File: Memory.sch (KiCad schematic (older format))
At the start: 20 parts, among them U10 DRAM_4464, U9 DRAM_4464

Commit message: SMD ram
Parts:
- R100, R101, R102, R103, R104, R105, R106, R107, R207, R208, R209, R210, R211, R212, R213, R214: footprint Atari:R_Axial_DIN0207_L3.6mm_D2.2mm_P10.16mm_Horizontal -> Resistor_SMD:R_1206_3216Metric_Pad1.42x1.75mm_HandSolder
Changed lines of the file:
@@
 F 0 "R207" V 2800 1175 50  0000 C CNN
 F 1 "33" V 2800 1350 50  0000 C CNN
-F 2 "Atari:R_Axial_DIN0207_L3.6mm_D2.2mm_P10.16mm_Horizontal" V 2830 1325 50  0001 C CNN
+F 2 "Resistor_SMD:R_1206_3216Metric_Pad1.42x1.75mm_HandSolder" V 2830 1325 50  0001 C CNN
 F 3 "~" H 2900 1325 50  0001 C CNN
 	1    2900 1325
@@
 F 0 "R208" V 2800 1350 50  0000 C CNN
 F 1 "33" V 2800 1525 50  0000 C CNN
-F 2 "Atari:R_Axial_DIN0207_L3.6mm_D2.2mm_P10.16mm_Horizontal" V 2830 1500 50  0001 C CNN
+F 2 "Resistor_SMD:R_1206_3216Metric_Pad1.42x1.75mm_HandSolder" V 2830 1500 50  0001 C CNN
 F 3 "~" H 2900 1500 50  0001 C CNN
 	1    2900 1500
@@
 F 0 "R209" V 2800 1550 50  0000 C CNN
 F 1 "33" V 2800 1725 50  0000 C CNN
-F 2 "Atari:R_Axial_DIN0207_L3.6mm_D2.2mm_P10.16mm_Horizontal" V 2830 1700 50  0001 C CNN
+F 2 "Resistor_SMD:R_1206_3216Metric_Pad1.42x1.75mm_HandSolder" V 2830 1700 50  0001 C CNN
 F 3 "~" H 2900 1700 50  0001 C CNN
 	1    2900 1700
@@
 F 0 "R210" V 2800 1750 50  0000 C CNN
 F 1 "33" V 2800 1925 50  0000 C CNN
-F 2 "Atari:R_Axial_DIN0207_L3.6mm_D2.2mm_P10.16mm_Horizontal" V 2830 1900 50  0001 C CNN
+F 2 "Resistor_SMD:R_1206_3216Metric_Pad1.42x1.75mm_HandSolder" V 2830 1900 50  0001 C CNN
 F 3 "~" H 2900 1900 50  0001 C CNN
 	1    2900 1900
@@
 F 0 "R211" V 2800 1950 50  0000 C CNN
 F 1 "33" V 2800 2125 50  0000 C CNN
-F 2 "Atari:R_Axial_DIN0207_L3.6mm_D2.2mm_P10.16mm_Horizontal" V 2830 2100 50  0001 C CNN
+F 2 "Resistor_SMD:R_1206_3216Metric_Pad1.42x1.75mm_HandSolder" V 2830 2100 50  0001 C CNN
 F 3 "~" H 2900 2100 50  0001 C CNN
 	1    2900 2100
@@
 F 0 "R212" V 2800 2150 50  0000 C CNN
 F 1 "33" V 2800 2325 50  0000 C CNN
-F 2 "Atari:R_Axial_DIN0207_L3.6mm_D2.2mm_P10.16mm_Horizontal" V 2830 2300 50  0001 C CNN
+F 2 "Resistor_SMD:R_1206_3216Metric_Pad1.42x1.75mm_HandSolder" V 2830 2300 50  0001 C CNN
 F 3 "~" H 2900 2300 50  0001 C CNN
 	1    2900 2300
@@
 F 0 "R213" V 2800 2350 50  0000 C CNN
 F 1 "33" V 2800 2525 50  0000 C CNN
-F 2 "Atari:R_Axial_DIN0207_L3.6mm_D2.2mm_P10.16mm_Horizontal" V 2830 2500 50  0001 C CNN
+F 2 "Resistor_SMD:R_1206_3216Metric_Pad1.42x1.75mm_HandSolder" V 2830 2500 50  0001 C CNN
 F 3 "~" H 2900 2500 50  0001 C CNN
 	1    2900 2500
@@
 F 0 "R214" V 2800 2550 50  0000 C CNN
 F 1 "33" V 2800 2725 50  0000 C CNN
-F 2 "Atari:R_Axial_DIN0207_L3.6mm_D2.2mm_P10.16mm_Horizontal" V 2830 2700 50  0001 C CNN
+F 2 "Resistor_SMD:R_1206_3216Metric_Pad1.42x1.75mm_HandSolder" V 2830 2700 50  0001 C CNN
 F 3 "~" H 2900 2700 50  0001 C CNN
 	1    2900 2700
@@
 F 0 "R100" V 2925 3775 50  0000 C CNN
 F 1 "10k" V 2875 3600 50  0000 C CNN
-F 2 "Atari:R_Axial_DIN0207_L3.6mm_D2.2mm_P10.16mm_Horizontal" V 2855 3775 50  0001 C CNN
+F 2 "Resistor_SMD:R_1206_3216Metric_Pad1.42x1.75mm_HandSolder" V 2855 3775 50  0001 C CNN
 F 3 "~" H 2925 3775 50  0001 C CNN
 	1    2925 3775
@@
 F 0 "R101" V 2925 3900 50  0000 C CNN
 F 1 "10k" V 2875 3725 50  0000 C CNN
-F 2 "Atari:R_Axial_DIN0207_L3.6mm_D2.2mm_P10.16mm_Horizontal" V 2855 3900 50  0001 C CNN
+F 2 "Resistor_SMD:R_1206_3216Metric_Pad1.42x1.75mm_HandSolder" V 2855 3900 50  0001 C CNN
 F 3 "~" H 2925 3900 50  0001 C CNN
 	1    2925 3900
@@
 F 0 "R102" V 2925 4025 50  0000 C CNN
 F 1 "10k" V 2875 3850 50  0000 C CNN
-F 2 "Atari:R_Axial_DIN0207_L3.6mm_D2.2mm_P10.16mm_Horizontal" V 2855 4025 50  0001 C CNN
+F 2 "Resistor_SMD:R_1206_3216Metric_Pad1.42x1.75mm_HandSolder" V 2855 4025 50  0001 C CNN
 F 3 "~" H 2925 4025 50  0001 C CNN
 	1    2925 4025
@@
 F 0 "R103" V 2925 4150 50  0000 C CNN
 F 1 "10k" V 2875 3975 50  0000 C CNN
-F 2 "Atari:R_Axial_DIN0207_L3.6mm_D2.2mm_P10.16mm_Horizontal" V 2855 4150 50  0001 C CNN
+F 2 "Resistor_SMD:R_1206_3216Metric_Pad1.42x1.75mm_HandSolder" V 2855 4150 50  0001 C CNN
 F 3 "~" H 2925 4150 50  0001 C CNN
 	1    2925 4150
@@
 F 0 "R104" V 2925 4275 50  0000 C CNN
 F 1 "10k" V 2875 4100 50  0000 C CNN
-F 2 "Atari:R_Axial_DIN0207_L3.6mm_D2.2mm_P10.16mm_Horizontal" V 2855 4275 50  0001 C CNN
+F 2 "Resistor_SMD:R_1206_3216Metric_Pad1.42x1.75mm_HandSolder" V 2855 4275 50  0001 C CNN
 F 3 "~" H 2925 4275 50  0001 C CNN
 	1    2925 4275
@@
 F 0 "R105" V 2925 4400 50  0000 C CNN
 F 1 "10k" V 2875 4225 50  0000 C CNN
-F 2 "Atari:R_Axial_DIN0207_L3.6mm_D2.2mm_P10.16mm_Horizontal" V 2855 4400 50  0001 C CNN
+F 2 "Resistor_SMD:R_1206_3216Metric_Pad1.42x1.75mm_HandSolder" V 2855 4400 50  0001 C CNN
 F 3 "~" H 2925 4400 50  0001 C CNN
 	1    2925 4400
@@
 F 0 "R106" V 2925 4525 50  0000 C CNN
 F 1 "10k" V 2875 4350 50  0000 C CNN
-F 2 "Atari:R_Axial_DIN0207_L3.6mm_D2.2mm_P10.16mm_Horizontal" V 2855 4525 50  0001 C CNN
+F 2 "Resistor_SMD:R_1206_3216Metric_Pad1.42x1.75mm_HandSolder" V 2855 4525 50  0001 C CNN
 F 3 "~" H 2925 4525 50  0001 C CNN
 	1    2925 4525
@@
 F 0 "R107" V 2925 4650 50  0000 C CNN
 F 1 "10k" V 2875 4475 50  0000 C CNN
-F 2 "Atari:R_Axial_DIN0207_L3.6mm_D2.2mm_P10.16mm_Horizontal" V 2855 4650 50  0001 C CNN
+F 2 "Resistor_SMD:R_1206_3216Metric_Pad1.42x1.75mm_HandSolder" V 2855 4650 50  0001 C CNN
 F 3 "~" H 2925 4650 50  0001 C CNN
 	1    2925 4650

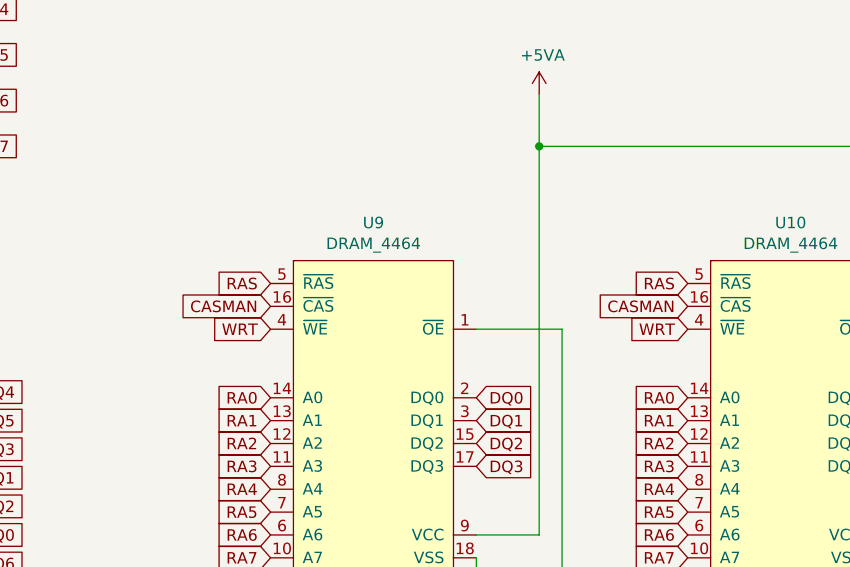
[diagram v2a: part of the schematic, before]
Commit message: add 74ls04
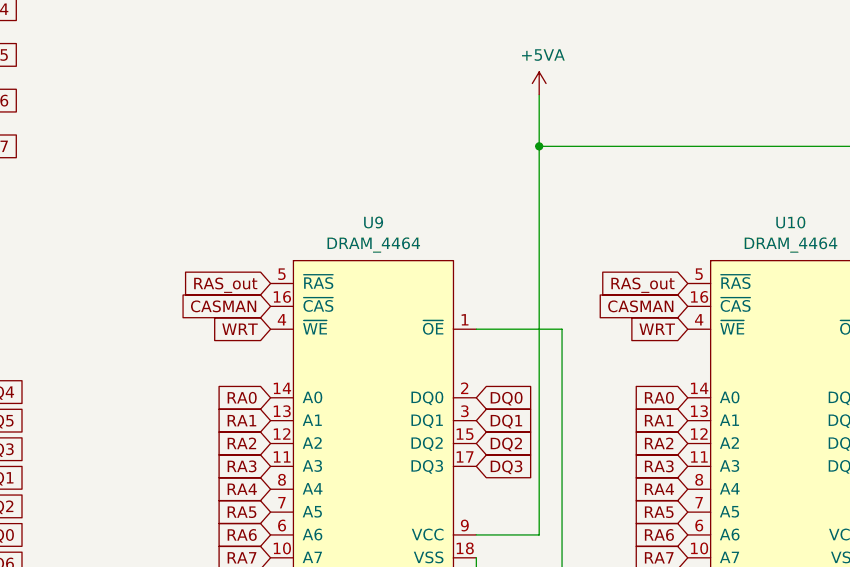
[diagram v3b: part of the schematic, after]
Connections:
- net RAS renamed RAS_out
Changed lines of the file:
@@
 $EndComp
 Text GLabel 4400 3300 0    50   Input ~ 0
-RAS
+RAS_out
 Text GLabel 4400 3500 0    50   Input ~ 0
 WRT
@@
 WRT
 Text GLabel 6225 3300 0    50   Input ~ 0
-RAS
+RAS_out
 Text GLabel 5300 3800 2    50   Input ~ 0
 DQ0

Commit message: Final inspection
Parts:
- C36, C37: footprint Capacitor_THT:C_Axial_L3.8mm_D2.6mm_P7.50mm_Horizontal -> Capacitor_SMD:C_1206_3216Metric_Pad1.42x1.75mm_HandSolder
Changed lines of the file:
@@
 F 0 "C37" H 6190 6096 50  0000 L CNN
 F 1 "100nF" H 6190 6005 50  0000 L CNN
-F 2 "Capacitor_THT:C_Axial_L3.8mm_D2.6mm_P7.50mm_Horizontal" H 6113 5900 50  0001 C CNN
+F 2 "Capacitor_SMD:C_1206_3216Metric_Pad1.42x1.75mm_HandSolder" H 6113 5900 50  0001 C CNN
 F 3 "~" H 6075 6050 50  0001 C CNN
 	1    6075 6050
@@
 F 0 "C36" H 6690 6096 50  0000 L CNN
 F 1 "100nF" H 6690 6005 50  0000 L CNN
-F 2 "Capacitor_THT:C_Axial_L3.8mm_D2.6mm_P7.50mm_Horizontal" H 6613 5900 50  0001 C CNN
+F 2 "Capacitor_SMD:C_1206_3216Metric_Pad1.42x1.75mm_HandSolder" H 6613 5900 50  0001 C CNN
 F 3 "~" H 6575 6050 50  0001 C CNN
 	1    6575 6050
